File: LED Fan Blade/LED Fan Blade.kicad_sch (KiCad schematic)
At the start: 28 parts

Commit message: Finished up PCB
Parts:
- added Boot: SW_Push, FanbladeFootprints:ButtonSMD, symbol Switch:SW_Push
- added C4: 47pF, Capacitor_SMD:C_0201_0603Metric, symbol Device:C
- added CB1: 100nF, Capacitor_SMD:C_0201_0603Metric, symbol Device:C
- added Cin1: 10uF, Capacitor_SMD:C_0201_0603Metric, symbol Device:C
- added Cout1: 47uF, Capacitor_SMD:C_0201_0603Metric, symbol Device:C
- added HallSensor: MRMS201A-001, FanbladeFootprints:XDCR_MRMS201A-001, symbol FanBladeSymbols:MRMS201A-001
- added L1: 2.4uH, Inductor_SMD:L_0201_0603Metric, symbol Device:L
- added Power_12V1: Power Terminal, FanbladeFootprints:Power_Terminal, symbol Connector:Screw_Terminal_01x02
- added R7: 100K, Resistor_SMD:R_0201_0603Metric, symbol Device:R
- added R8: 21.5k, Resistor_SMD:R_0201_0603Metric, symbol Device:R
- added R9: 5.11K, Resistor_SMD:R_0201_0603Metric, symbol Device:R
- added VReg: ~, FanbladeFootprints:AN_SY8105, symbol FanBladeSymbols:SY8105ADC
- BL:0, BL:1, BL:2, BL:3, BL:4, BL:5: value 10K -> 5 Ω
- GR:0, GR:1, GR:2, GR:3, GR:4, GR:5: value 10K -> 15 Ω
- RD:0, RD:1, RD:2, RD:3, RD:4, RD:5: value 10K -> 65 Ω
- renumbered CapVCAP1 to VCAP1
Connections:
- net +5V is gone; now on net +3.3V: LED-Driver1.16 (VLED), LED-Driver1.40 (VCC)
- net +3.3V: now also ESP1.2 (EN), C4.1, Cout1.1, HallSensor.1 (VCC), L1.2, R7.1; no longer R2.1
- net GND: now also R2.1, Cin1.2, Cout1.2, HallSensor.2 (GND), Power_12V1.2 (Pin_2), R8.2, R9.1, VReg.3 (GND)
- net at R2.2: now also Boot.2; no longer ESP1.2 (EN)
- net at USB-C1.A4 (VBUS), USB-C1.A9 (VBUS), USB-C1.B4 (VBUS)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: now also R9.2
- net Hall Sense: now reaches ESP1.15 (IO3)
- net Hall Sense: now also HallSensor.3 (OUT)
- net at ESP1.8 (IO9): now also Boot.1
- new net: CB1.2, L1.1, VReg.5 (LX)
- new net: CB1.1, VReg.6 (BS)
- new net: C4.2, R7.2, R8.1, VReg.1 (FB)
- new net +12V: Cin1.1, Power_12V1.1 (Pin_1), VReg.2 (EN), VReg.4 (IN)
- no-connect marks 14 -> 11
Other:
- moved on the sheet: R5

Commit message: Changed PCB
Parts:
- BL:0, BL:1, BL:2, BL:3, BL:4, BL:5: value 5 Ω -> 5; footprint Resistor_SMD:R_0201_0603Metric -> FanbladeFootprints:Resistor_603
- C4, CB1, Cin1, Cout1, VCAP1: footprint Capacitor_SMD:C_0201_0603Metric -> FanbladeFootprints:Cap_603
- GR:0, GR:1, GR:2, GR:3, GR:4, GR:5: value 15 Ω -> 15; footprint Resistor_SMD:R_0201_0603Metric -> FanbladeFootprints:Resistor_603
- L1: footprint Inductor_SMD:L_0201_0603Metric -> FanbladeFootprints:Inductor_Sunlord
- R1, R2, R3, R4, R5, R6, R7, R8, R9: footprint Resistor_SMD:R_0201_0603Metric -> FanbladeFootprints:Resistor_603
- RD:0, RD:1, RD:2, RD:3, RD:4, RD:5: value 65 Ω -> 65; footprint Resistor_SMD:R_0201_0603Metric -> FanbladeFootprints:Resistor_603
- renumbered Boot to Boot1, HallSensor to HallSensor1, VReg to VReg1

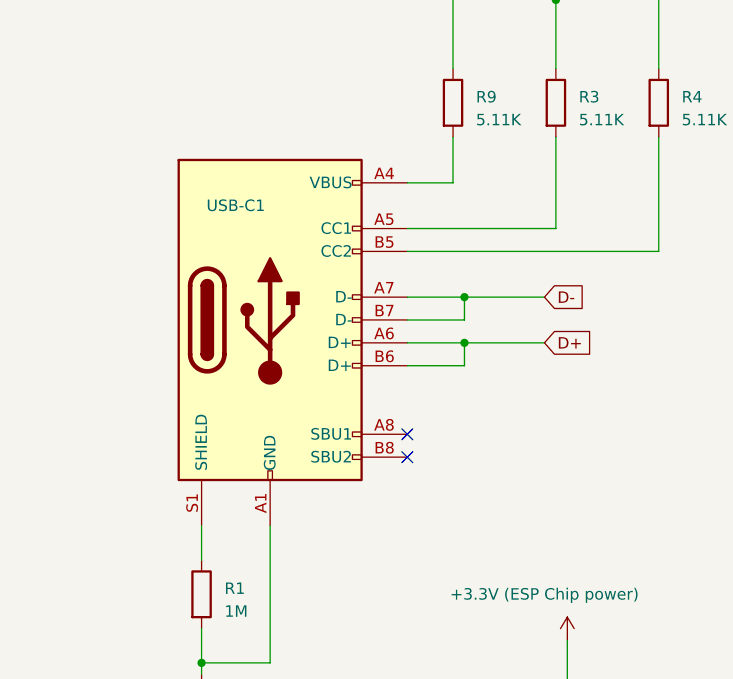
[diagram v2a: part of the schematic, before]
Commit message: Changed USB C connector to different one
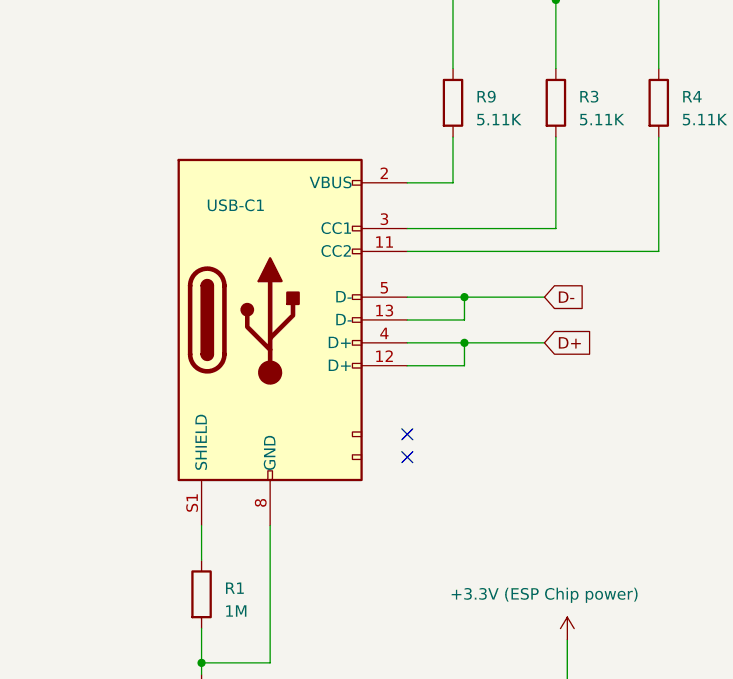
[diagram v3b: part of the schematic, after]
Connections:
- net D+: now also USB-C1.12 (D+), USB-C1.4 (D+); no longer USB-C1.A6 (D+), USB-C1.B6 (D+)
- net D-: now also USB-C1.13 (D-), USB-C1.5 (D-); no longer USB-C1.A7 (D-), USB-C1.B7 (D-)
- net GND: now also USB-C1.1 (GND), USB-C1.16 (GND), USB-C1.8 (GND), USB-C1.9 (GND); no longer USB-C1.A1 (GND), USB-C1.A12 (GND), USB-C1.B1 (GND), USB-C1.B12 (GND)
- net at R3.2: now also USB-C1.3 (CC1); no longer USB-C1.A5 (CC1)
- net at R4.2: now also USB-C1.11 (CC2); no longer USB-C1.B5 (CC2)
- new net: R9.2, USB-C1.10 (VBUS), USB-C1.15 (VBUS), USB-C1.2 (VBUS), USB-C1.7 (VBUS)
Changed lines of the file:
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@@
       (effects (font (size 1.27 1.27)) hide)
     )
-    (property "Footprint" "FanbladeFootprints:TYPE-C-31-M-14" (at 33.02 63.5 0)
+    (property "Footprint" "FanbladeFootprints:TYPE-C-31-M-14" (at 49.53 87.63 0)
       (effects (font (size 1.27 1.27)) hide)
     )
-    (property "Datasheet" "https://www.usb.org/sites/default/files/documents/usb_type-c.zip" (at 33.02 63.5 0)
+    (property "Datasheet" "!" (at 44.45 83.82 0)
       (effects (font (size 1.27 1.27)) hide)
     )
-    (pin "A1")
-    (pin "A12")
-    (pin "A4")
-    (pin "A5")
-    (pin "A6")
-    (pin "A7")
-    (pin "A8")
-    (pin "A9")
-    (pin "B1")
-    (pin "B12")
-    (pin "B4")
-    (pin "B5")
-    (pin "B6")
-    (pin "B7")
-    (pin "B8")
-    (pin "B9")
+    (pin "8")
+    (pin "9")
+    (pin "2")
+    (pin "3")
+    (pin "4")
+    (pin "5")
+    (pin "15")
+    (pin "1")
+    (pin "16")
+    (pin "10")
+    (pin "11")
+    (pin "12")
+    (pin "13")
+    (pin "7")
     (pin "S1")
     (instances
